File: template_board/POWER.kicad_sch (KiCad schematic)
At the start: 31 parts, among them IC3 LMR16030SDDAR, J2 Conn_01x02, J6 Conn_01x02, U4 AZ1117-3.3

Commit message: u5 wip
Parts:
- removed C25, C34, C35, C43: 100n, Capacitor_SMD:C_0402_1005Metric, symbol Device:C
- removed C46, C48: 2.2u, Capacitor_SMD:C_1206_3216Metric, symbol Device:C
- removed C47: 47u, Capacitor_SMD:C_Elec_10x10.2, symbol Device:C
- removed C49, C51: 47u, Capacitor_SMD:C_1206_3216Metric, symbol Device:C
- removed D6: SS34, Diode_SMD:D_SMA, symbol Diode:SS34
- removed IC3: LMR16030SDDAR, parts:SOIC127P600X170-9N, symbol LMR16030SDDAR:LMR16030SDDAR
- removed L2: 8.2u, Inductor_SMD:L_Cenker_CKCS6045, symbol Device:L
- removed R37: 49,9k, Resistor_SMD:R_0402_1005Metric, symbol Device:R
- removed R56: 100k, Resistor_SMD:R_0402_1005Metric, symbol Device:R
- removed R57: 17,8k, Resistor_SMD:R_0402_1005Metric, symbol Device:R
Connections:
- net +5V: now also R27.1
- net VCC: no longer R27.1
- no-connect marks 1 -> 0
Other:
- note removed: "1%"
- moved on the sheet: D7, R27, R29, R30

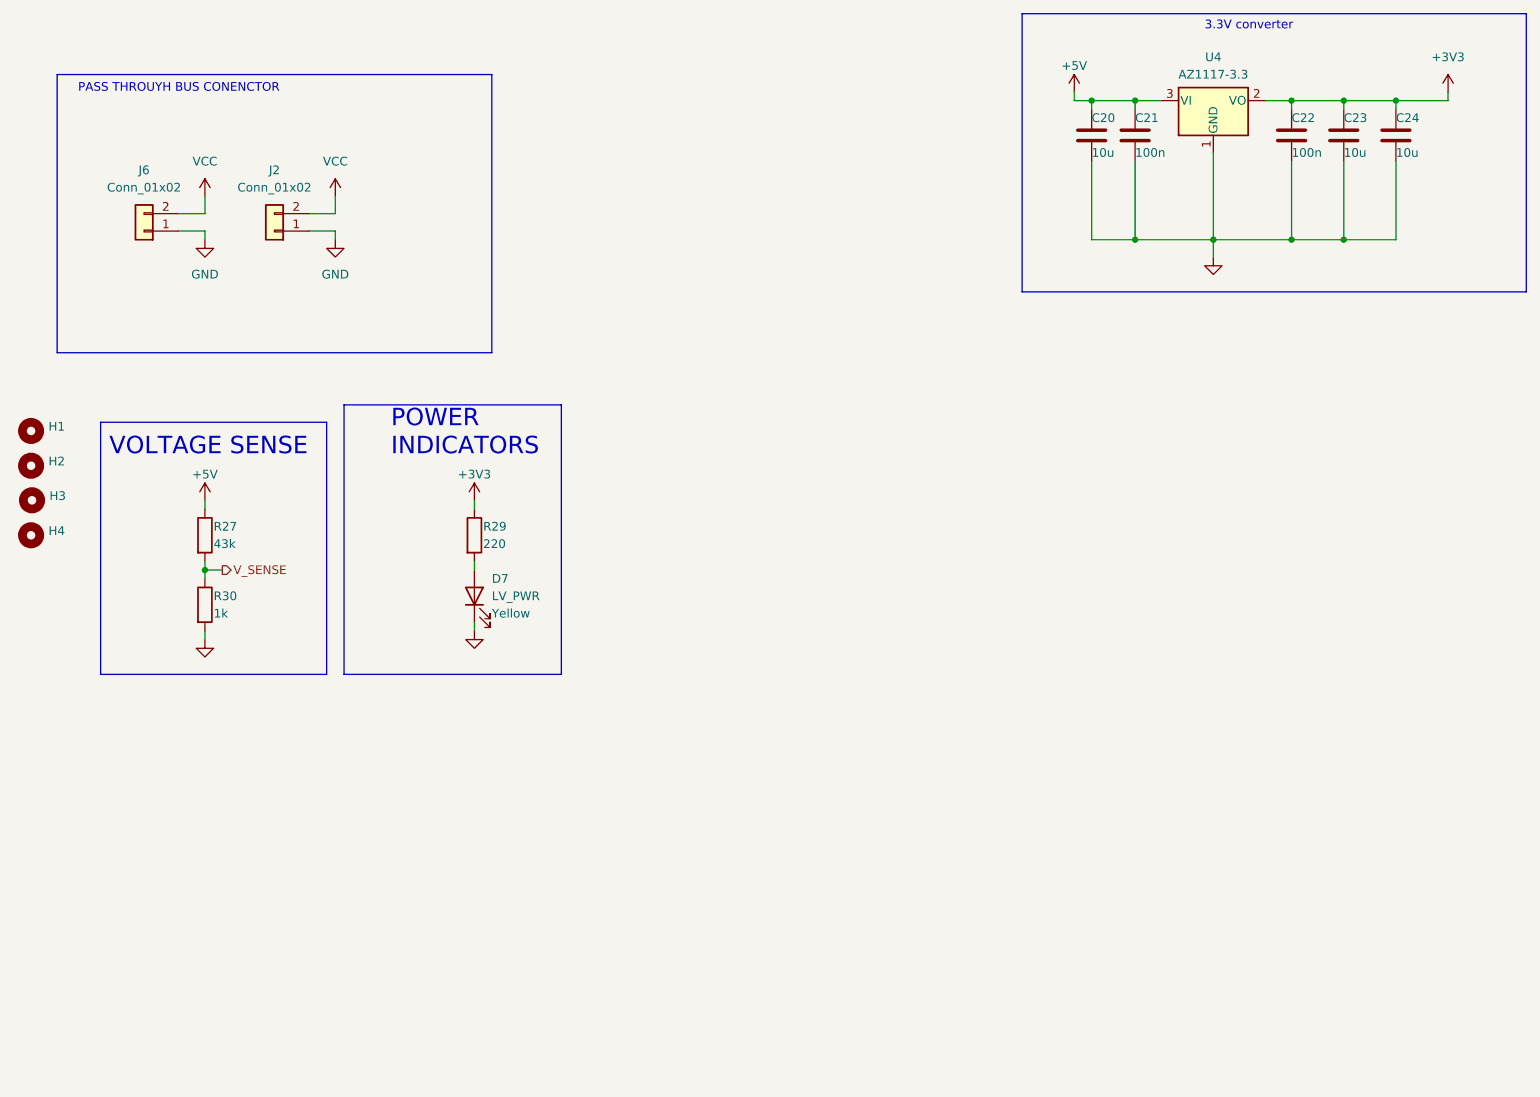
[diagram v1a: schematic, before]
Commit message: updated all subschematics
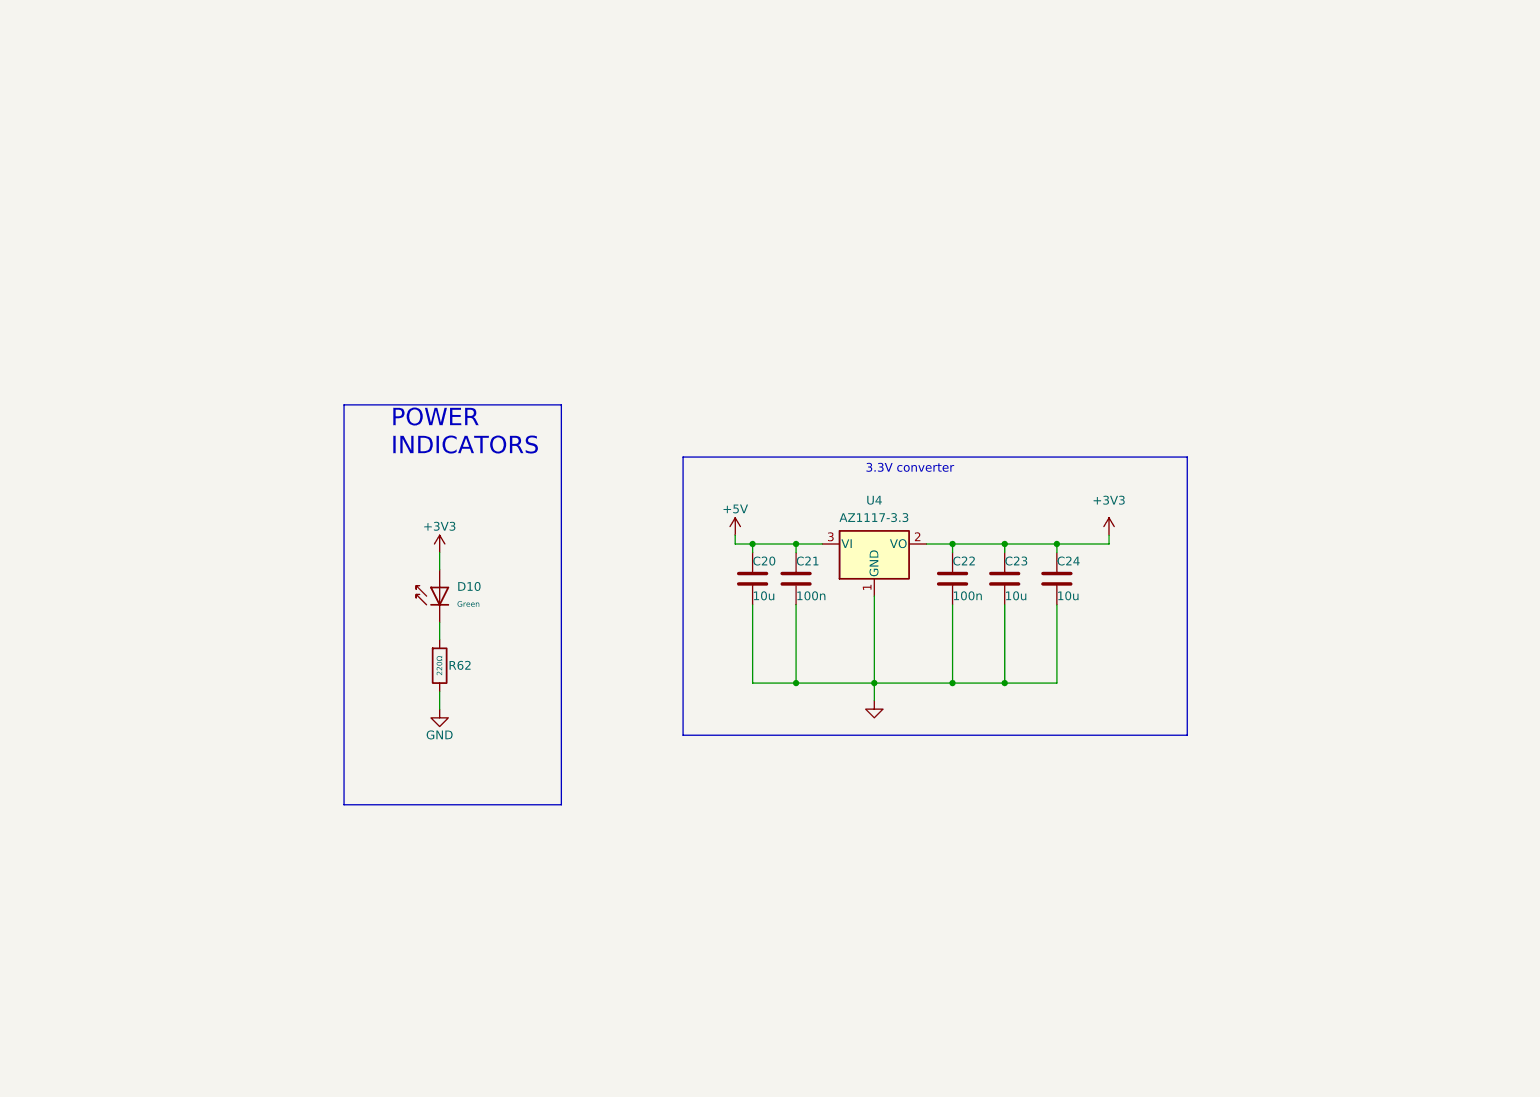
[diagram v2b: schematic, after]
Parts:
- removed D7: LV_PWR, Diode_SMD:D_0603_1608Metric, symbol Device:LED
- removed H1, H2, H3, H4: ~, MountingHole:MountingHole_3.2mm_M3, symbol Mechanical:MountingHole
- removed J2, J6: Conn_01x02, Connector_AMASS:AMASS_XT60PW-M_1x02_P7.20mm_Horizontal, symbol Connector_Generic:Conn_01x02
- removed R27: 43k, Resistor_SMD:R_0402_1005Metric, symbol Device:R
- removed R29: 220, Resistor_SMD:R_0402_1005Metric, symbol Device:R
- removed R30: 1k, Resistor_SMD:R_0402_1005Metric, symbol Device:R
- added D10: Green, PCM_JLCPCB:D_0603, symbol PCM_JLCPCB-Diodes:LED,0603,Green
- added R62: 220Ω, PCM_JLCPCB:R_0402, symbol PCM_JLCPCB-Resistors:0402,220Ω
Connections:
- net +3V3: now also D10.2
- net GND: now also R62.2
- new net: D10.1, R62.1
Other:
- note removed: "PASS THROUYH BUS CONENCTOR"
- note removed: "VOLTAGE SENSE"
- moved on the sheet: C20, C21, C22, C23, C24, U4

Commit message: can transiver update
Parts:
- removed C20, C23, C24: 10u, Capacitor_SMD:C_0805_2012Metric, symbol Device:C
- removed C21: 100n, Capacitor_SMD:C_0402_1005Metric, symbol Device:C
- removed C22: 100n, Capacitor_SMD:C_0603_1608Metric, symbol Device:C
- added C11, C14, C15: 10uF, PCM_JLCPCB:C_0402, symbol PCM_JLCPCB-Capacitors:0402,10uF
- added C12, C13: 100nF, PCM_JLCPCB:C_0402, symbol PCM_JLCPCB-Capacitors:0402,100nF
- added Q1: DMN2040U, Package_TO_SOT_SMD:SOT-23, symbol Transistor_FET:DMN2040U
- added R1: 10kΩ, PCM_JLCPCB:R_0402, symbol PCM_JLCPCB-Resistors:0402,10kΩ
- added R6: 1kΩ, PCM_JLCPCB:R_0402, symbol PCM_JLCPCB-Resistors:0402,1kΩ
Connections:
- net +3V3: now also C13.1, C14.1, C15.1
- net +5V: now also C11.1, C12.1, Q1.3 (D)
- net GND: now also C11.2, C12.2, C13.2, C14.2, C15.2, Q1.2 (S), R1.2
- new net: Q1.1 (G), R1.1, R6.2
- new net POWER_EN: R6.1
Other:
- moved on the sheet: U4

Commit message: chamt skończony chyba
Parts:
- removed Q1: DMN2040U, Package_TO_SOT_SMD:SOT-23, symbol Transistor_FET:DMN2040U
- removed R1: 10kΩ, PCM_JLCPCB:R_0402, symbol PCM_JLCPCB-Resistors:0402,10kΩ
- removed R6: 1kΩ, PCM_JLCPCB:R_0402, symbol PCM_JLCPCB-Resistors:0402,1kΩ
- added C16: 100nF 50V Y5V, Capacitor_SMD:C_0402_1005Metric, symbol Device:C_Small
- added D1: Green, PCM_JLCPCB:D_0603, symbol PCM_JLCPCB-Diodes:LED,0603,Green
- added Q3: AO3400A, Package_TO_SOT_SMD:SOT-23, symbol Transistor_FET:AO3400A
- added R1: 220Ω, PCM_JLCPCB:R_0402, symbol PCM_JLCPCB-Resistors:0402,220Ω
- added R11: 10kΩ, PCM_JLCPCB:R_0402, symbol PCM_JLCPCB-Resistors:0402,10kΩ
- added R14: 1kΩ, PCM_JLCPCB:R_0402, symbol PCM_JLCPCB-Resistors:0402,1kΩ
- added U2: LM74700, Package_TO_SOT_SMD:SOT-23-6, symbol Power_Management:LM74700
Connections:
- net +5V: now also Q3.3 (D), U2.4 (CATHODE)
- net GND: now also R1.2, R11.2, U2.2 (GND)
- net POWER_EN: now also R14.1
- new net: C16.2, U2.1 (VCAP)
- new net: D1.1, R1.1
- new net: R11.1, R14.2, U2.3 (EN)
- new net: Q3.1 (G), U2.5 (GATE)
- new net +5V_unprotected: C16.1, D1.2, Q3.2 (S), U2.6 (ANODE)
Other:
- note added: "3V3 DC/DC"
- note added: "POWER ON SWITCH"
- note removed: "3.3V converter"
- moved on the sheet: C11, C12, C13, C14, C15, D10, R62, U4

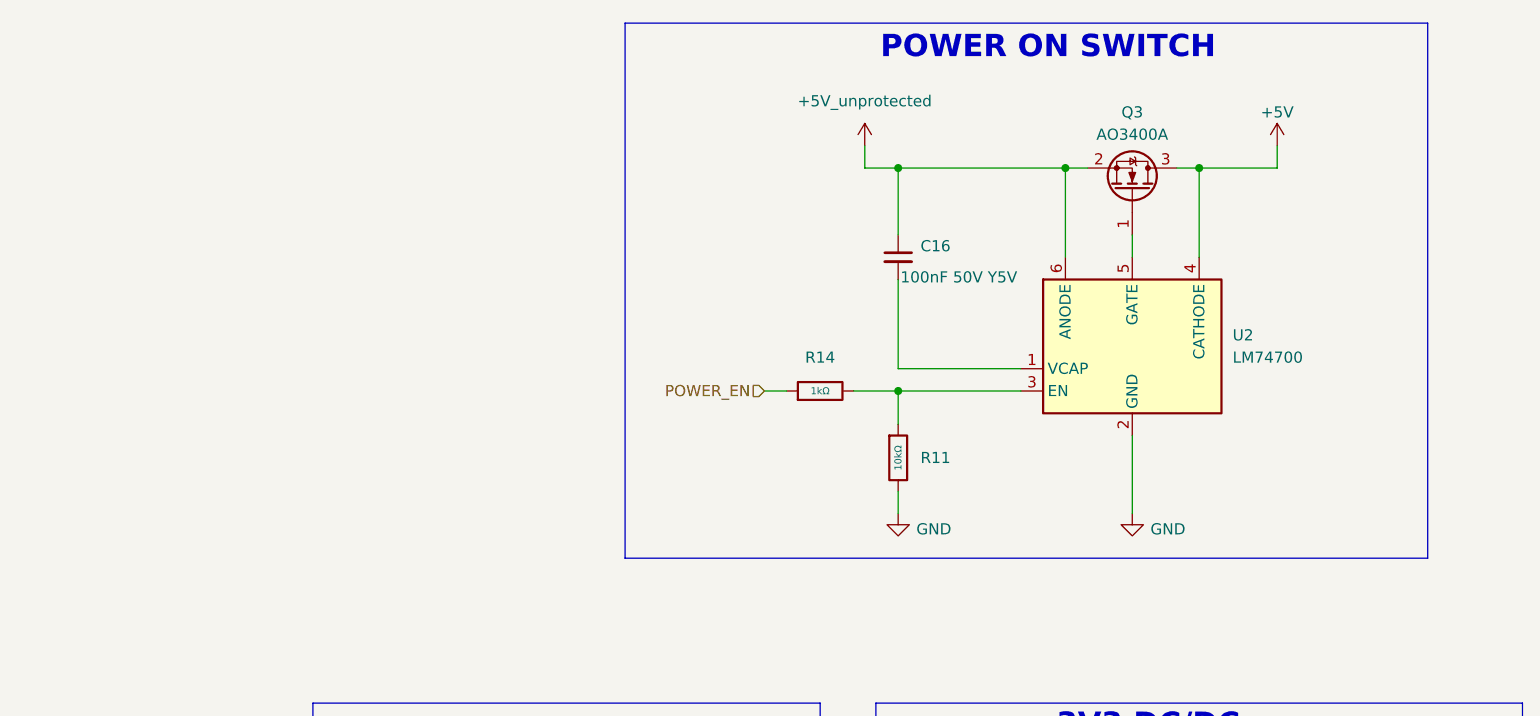
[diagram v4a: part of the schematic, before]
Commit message: sub leyoyut partially completed
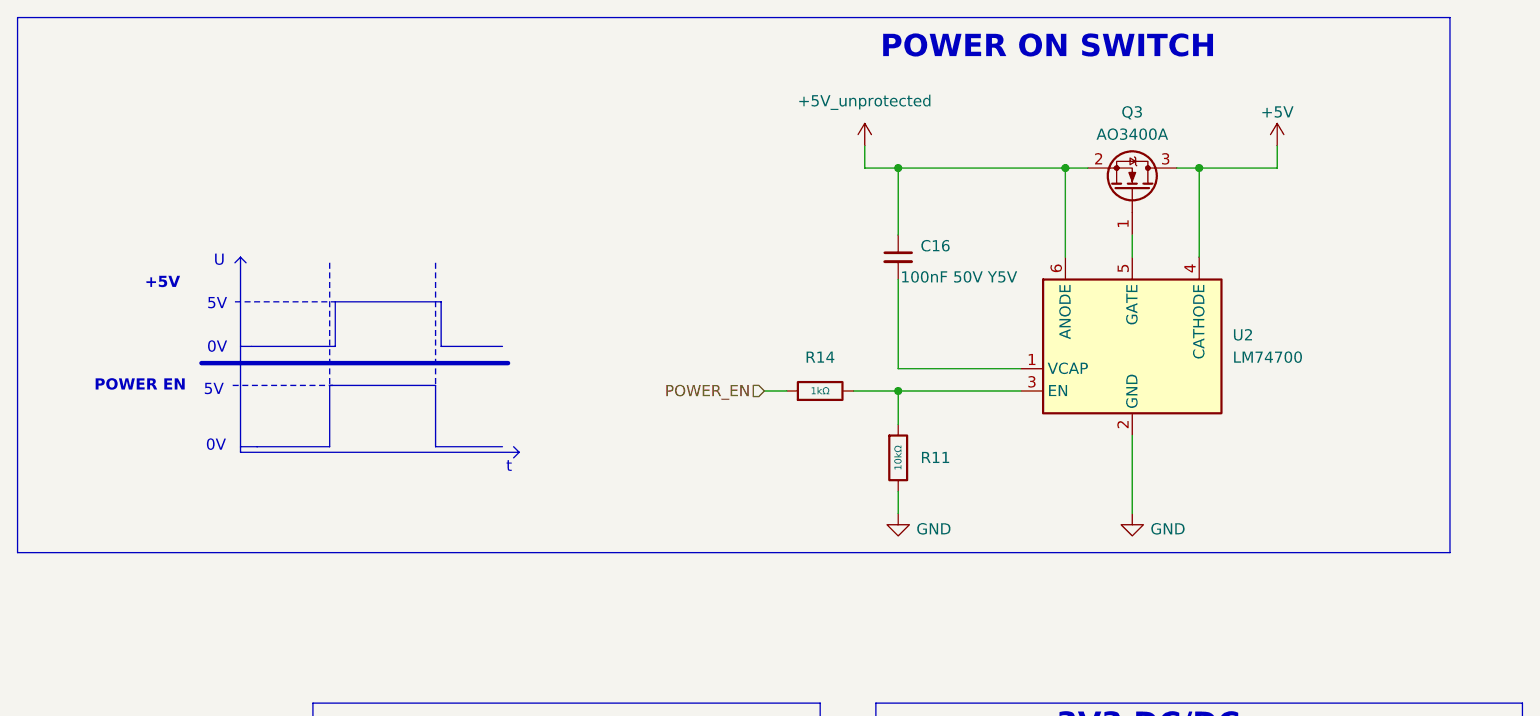
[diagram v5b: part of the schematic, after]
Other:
- note added: "+5V"
- note added: "0V"
- note added: "5V"
- note added: "POWER EN"
- note added: "U"
- note added: "t"
